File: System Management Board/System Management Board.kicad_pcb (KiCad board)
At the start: 2 copper layers, 116.8 x 142.2 mm, 9 parts, among them J6 Conn_02x20_Odd_Even, K1 J115F11CH5VDCS61.5U, K2 J114FL1CS165VDC.41, K3 J114FL1CS165VDC.41, U1 SC0915, U2 OKI-78SR-5/1.5-W36E-C, U3 OKI-78SR-5/1.5-W36E-C

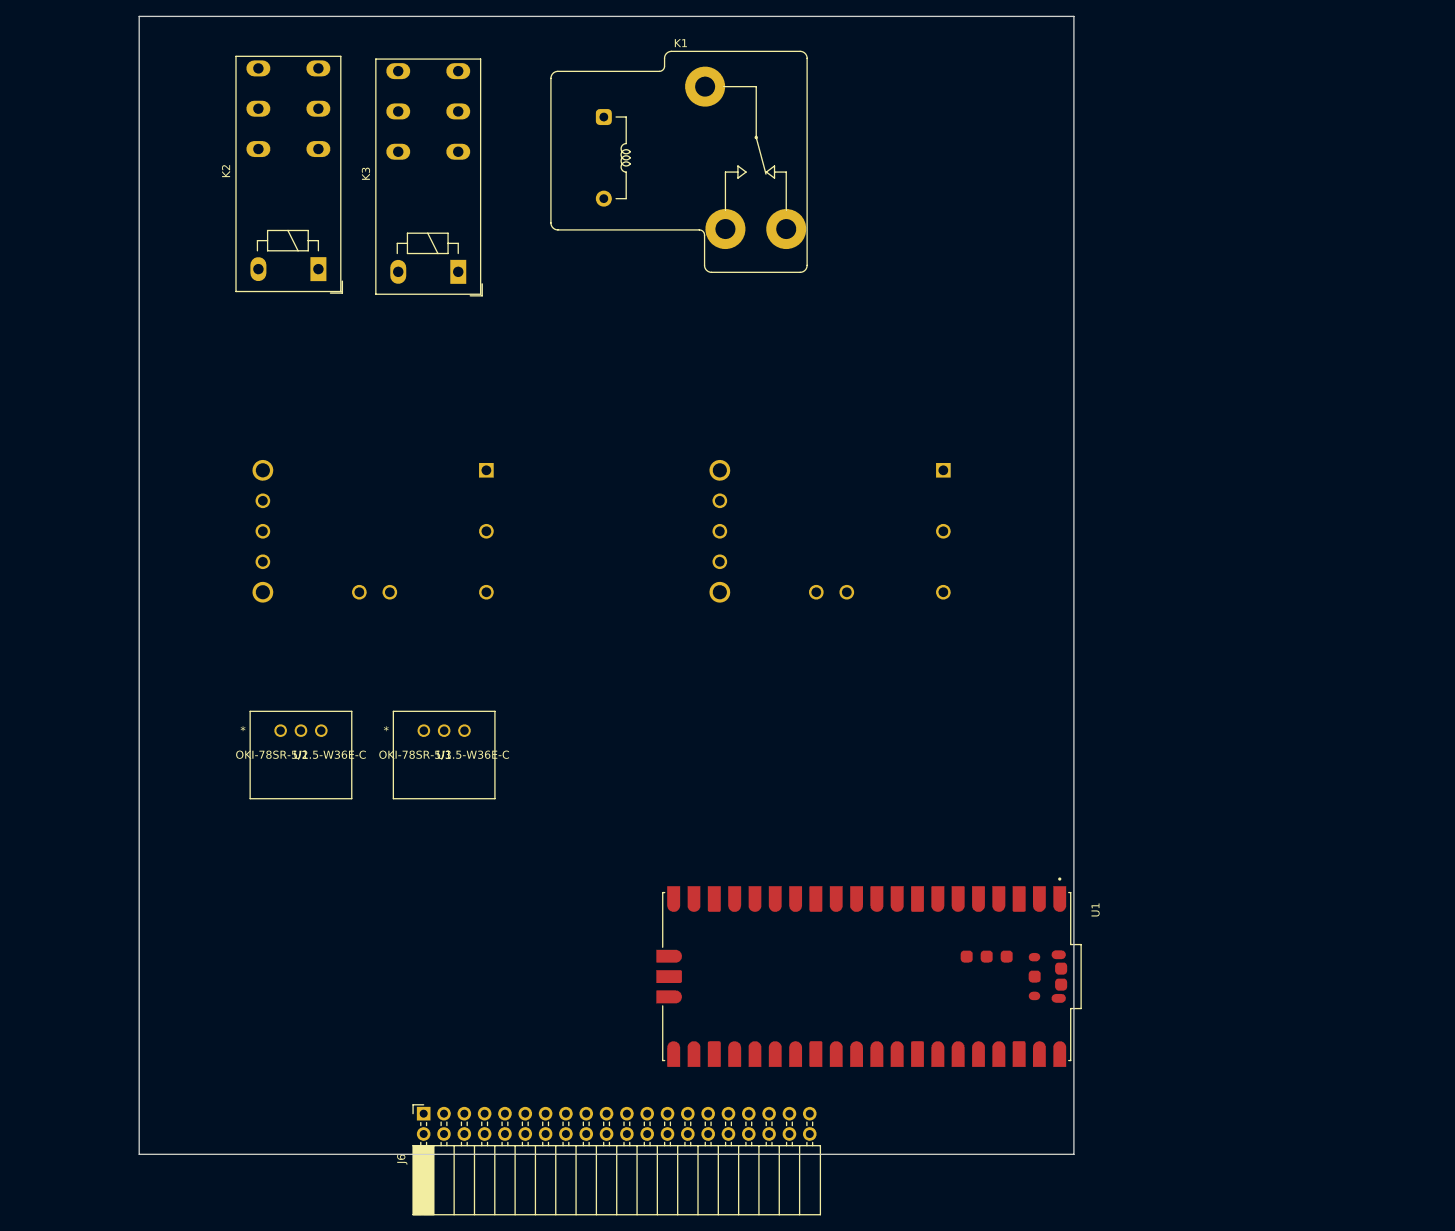
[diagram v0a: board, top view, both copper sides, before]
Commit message: Fixed solidworks brainmelt from last commit and moved PCb template into Kicad
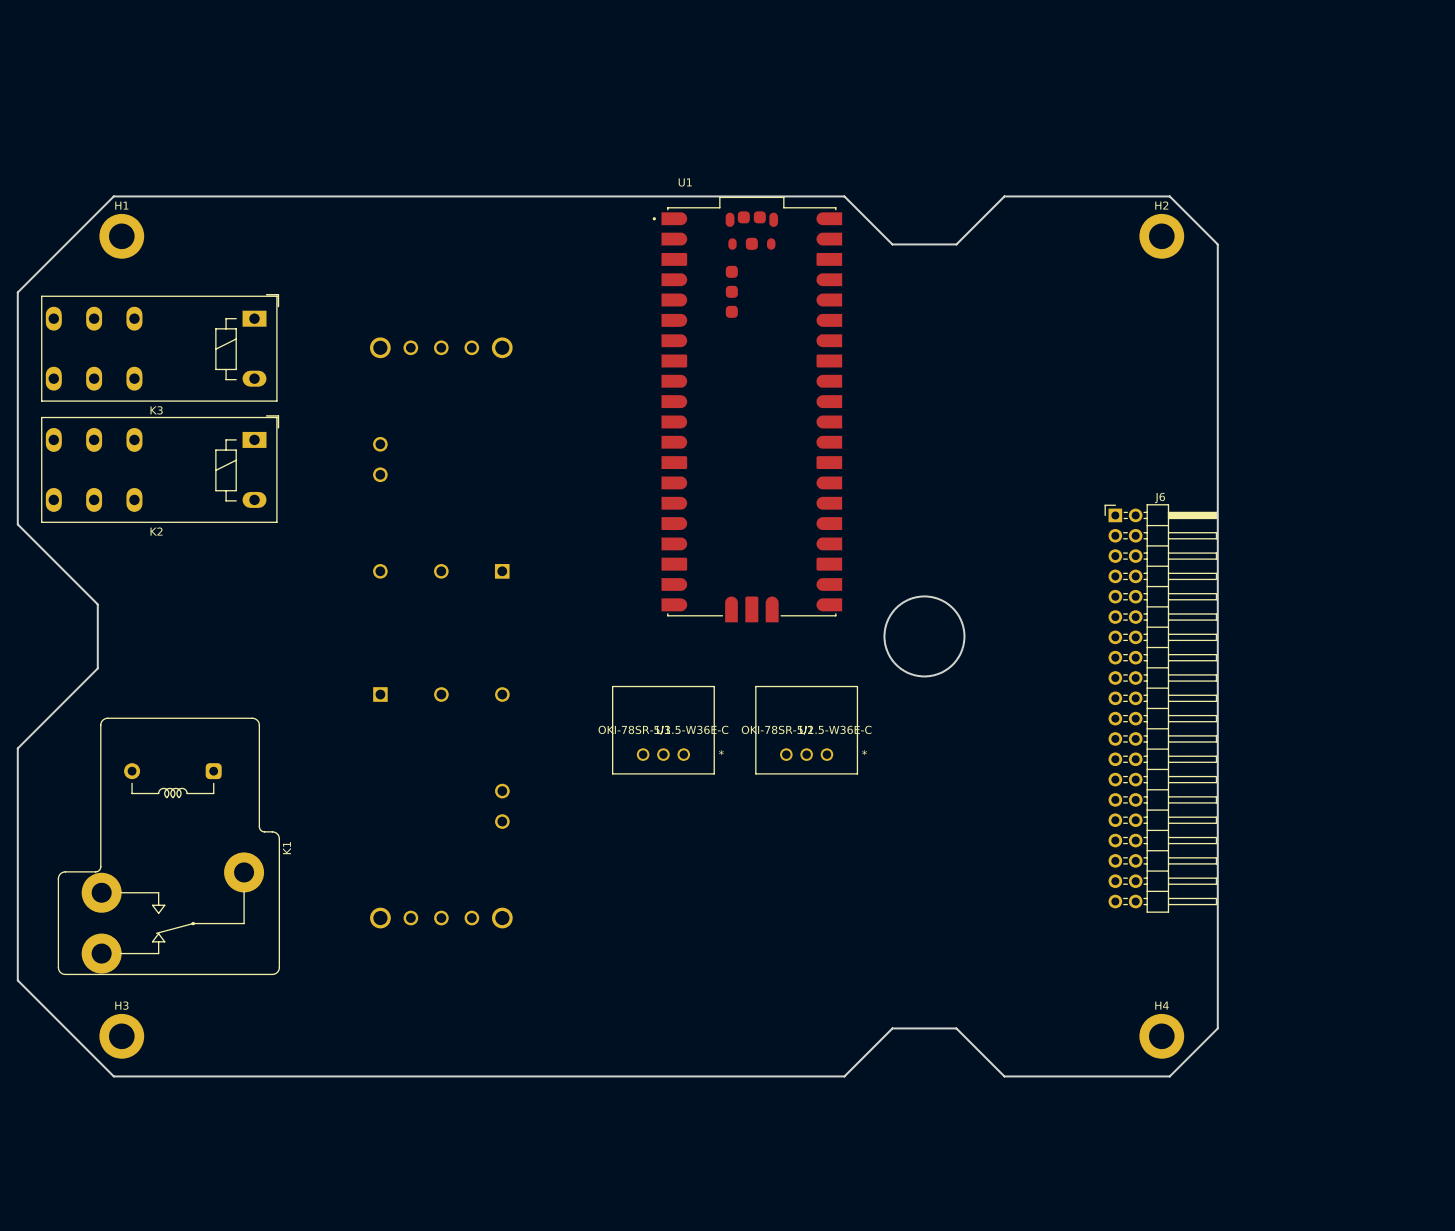
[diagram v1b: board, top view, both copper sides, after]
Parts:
- added H1: MountingHole_Pad, MountingHole:MountingHole_3.2mm_M3_DIN965_Pad, F.Cu at (86.7, 50.4)
- added H2: MountingHole_Pad, MountingHole:MountingHole_3.2mm_M3_DIN965_Pad, F.Cu at (216.7, 50.4)
- added H3: MountingHole_Pad, MountingHole:MountingHole_3.2mm_M3_DIN965_Pad, F.Cu at (86.7, 150.3)
- added H4: MountingHole_Pad, MountingHole:MountingHole_3.2mm_M3_DIN965_Pad, F.Cu at (216.7, 150.3)
- J6: footprint Connector_PinSocket_2.54mm:PinSocket_2x20_P2.54mm_Horizontal -> Connector_PinHeader_2.54mm:PinHeader_2x20_P2.54mm_Horizontal
- moved J6 114.3 mm to (210.9, 85.2), turned to 0 degrees
- moved K1 90.2 mm to (93.1, 114.7), turned to -90 degrees
- moved PS2 75.7 mm to (119.1, 107.6), turned to -90 degrees
- moved U1 72.0 mm to (165.5, 72.3), turned to 0 degrees
- moved U2 68.4 mm to (174.9, 115.1), turned to 180 degrees
- moved U3 32.6 mm to (157.0, 115.1), turned to 180 degrees
- moved K3 25.8 mm to (103.6, 60.6), turned to 180 degrees
- moved K2 22.5 mm to (103.6, 75.8), turned to 180 degrees
- moved PS1 12.8 mm to (134.3, 92.2), turned to 90 degrees
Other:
- board size 116.8 x 142.2 mm -> 150 x 110 mm
- copper layers 2 -> 4

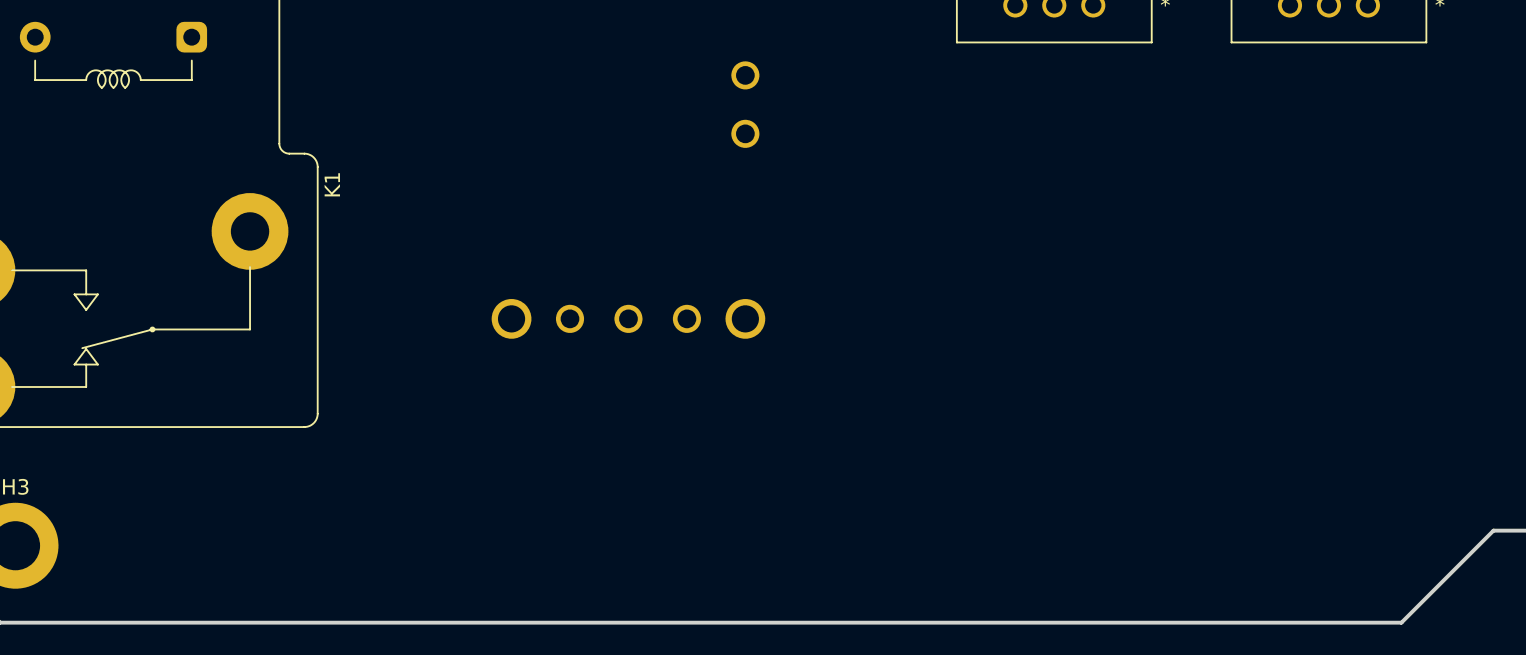
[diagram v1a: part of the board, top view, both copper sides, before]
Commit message: Worked on importing KiCad parts and major componet layout
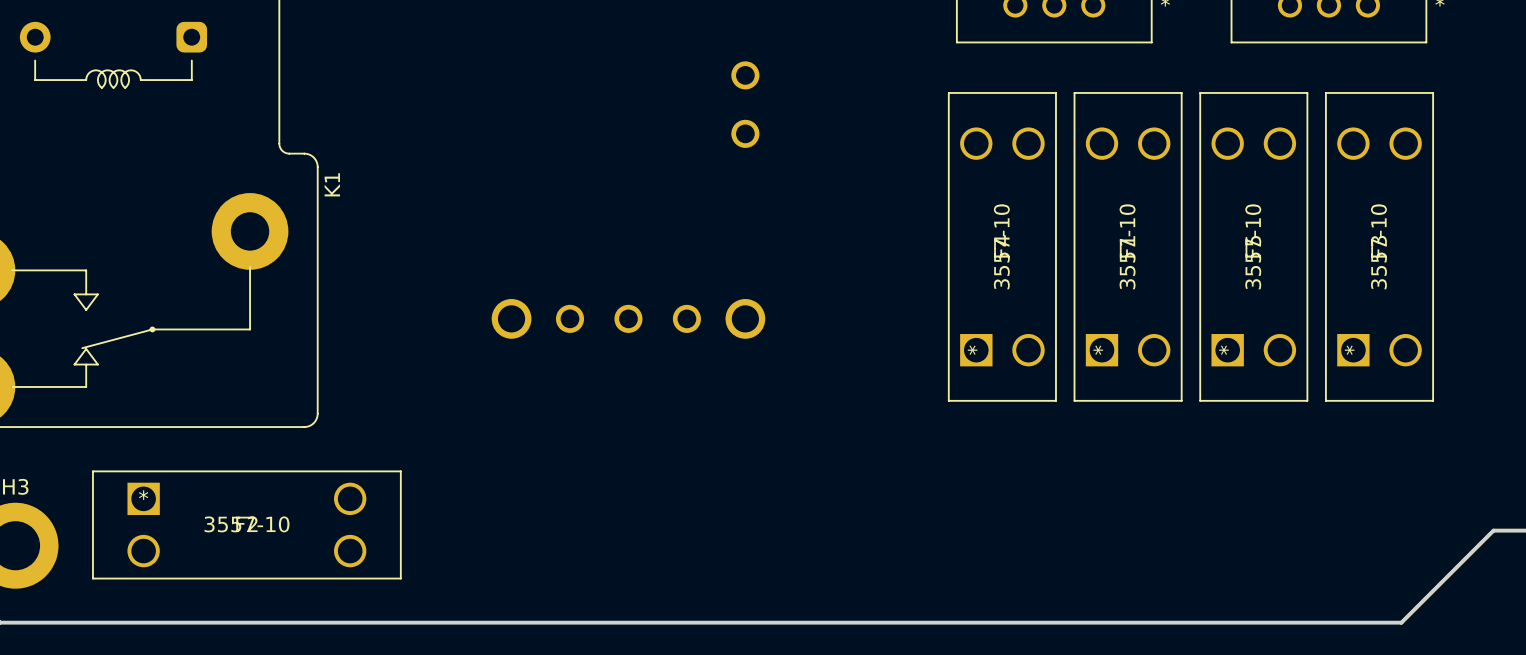
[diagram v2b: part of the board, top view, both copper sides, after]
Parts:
- added F1: 3557-10, SMB:3557-10, F.Cu at (157.5, 137.6)
- added F2: 3557-10, SMB:3557-10, F.Cu at (95.1, 147.3)
- added F3: 3557-10, SMB:3557-10, F.Cu at (173.9, 137.6)
- added F4: 3557-10, SMB:3557-10, F.Cu at (149.3, 137.6)
- added F5: 3557-10, SMB:3557-10, F.Cu at (165.7, 137.6)

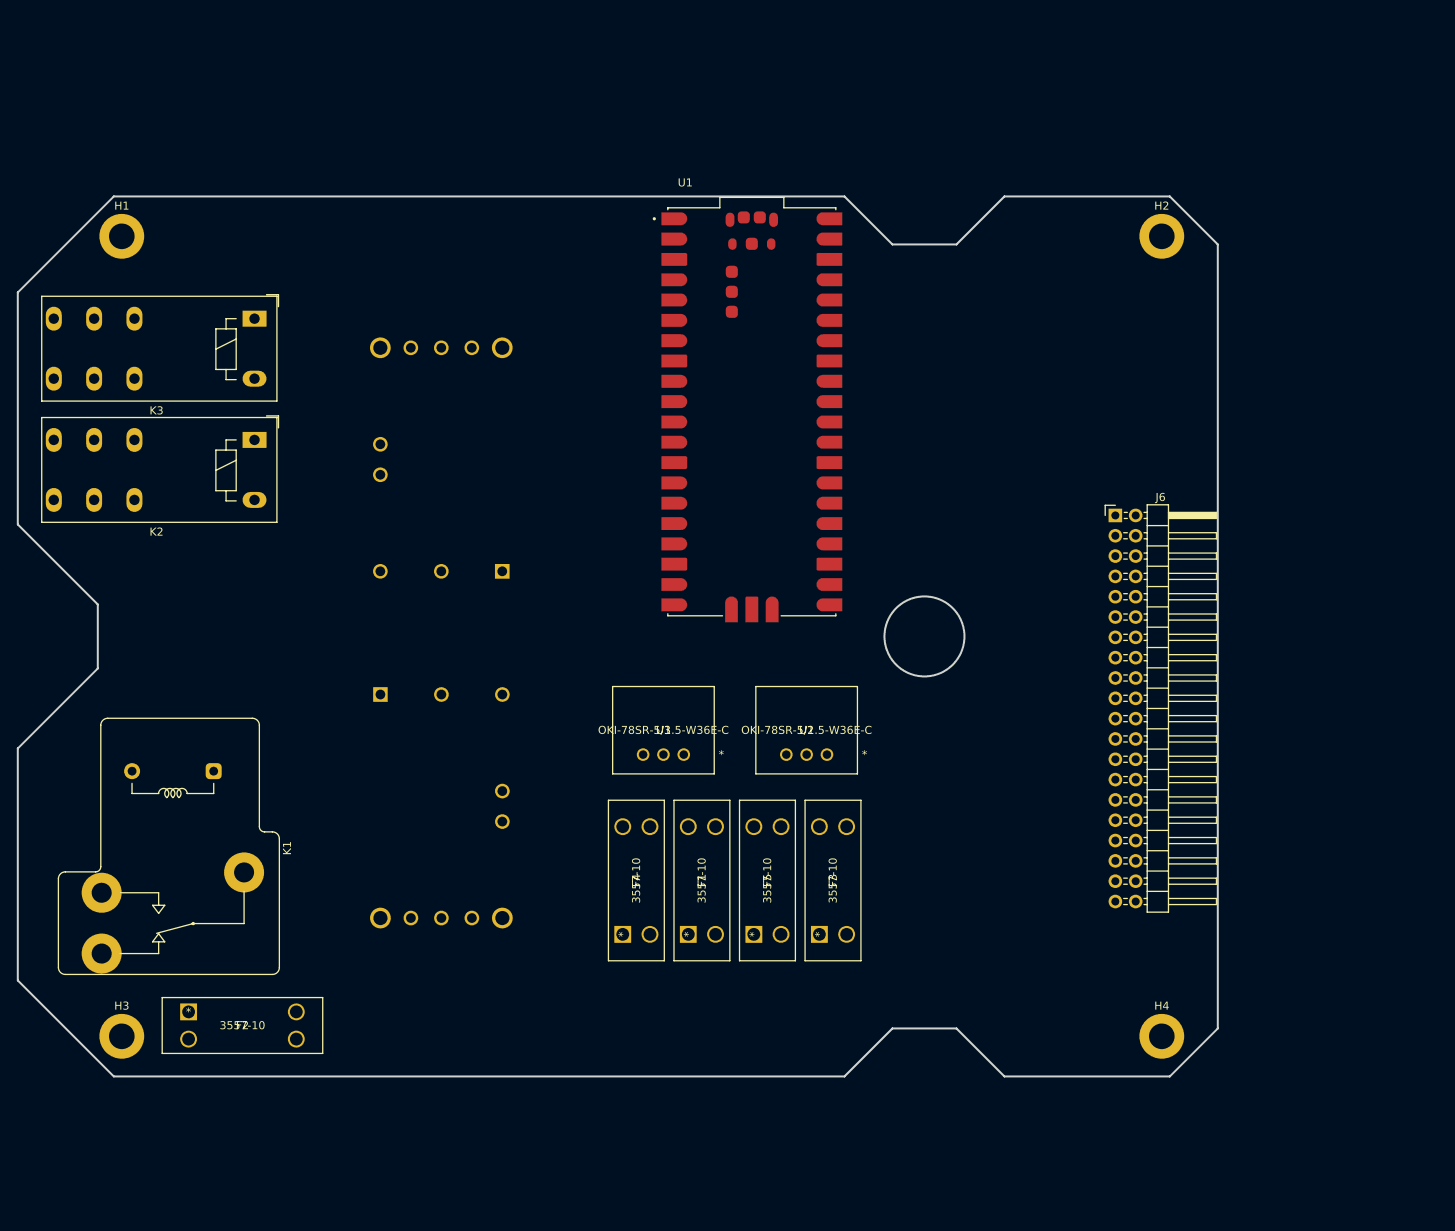
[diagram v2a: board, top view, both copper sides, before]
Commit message: Added more parts to SMB KiCad, worked on schematic and power supplies
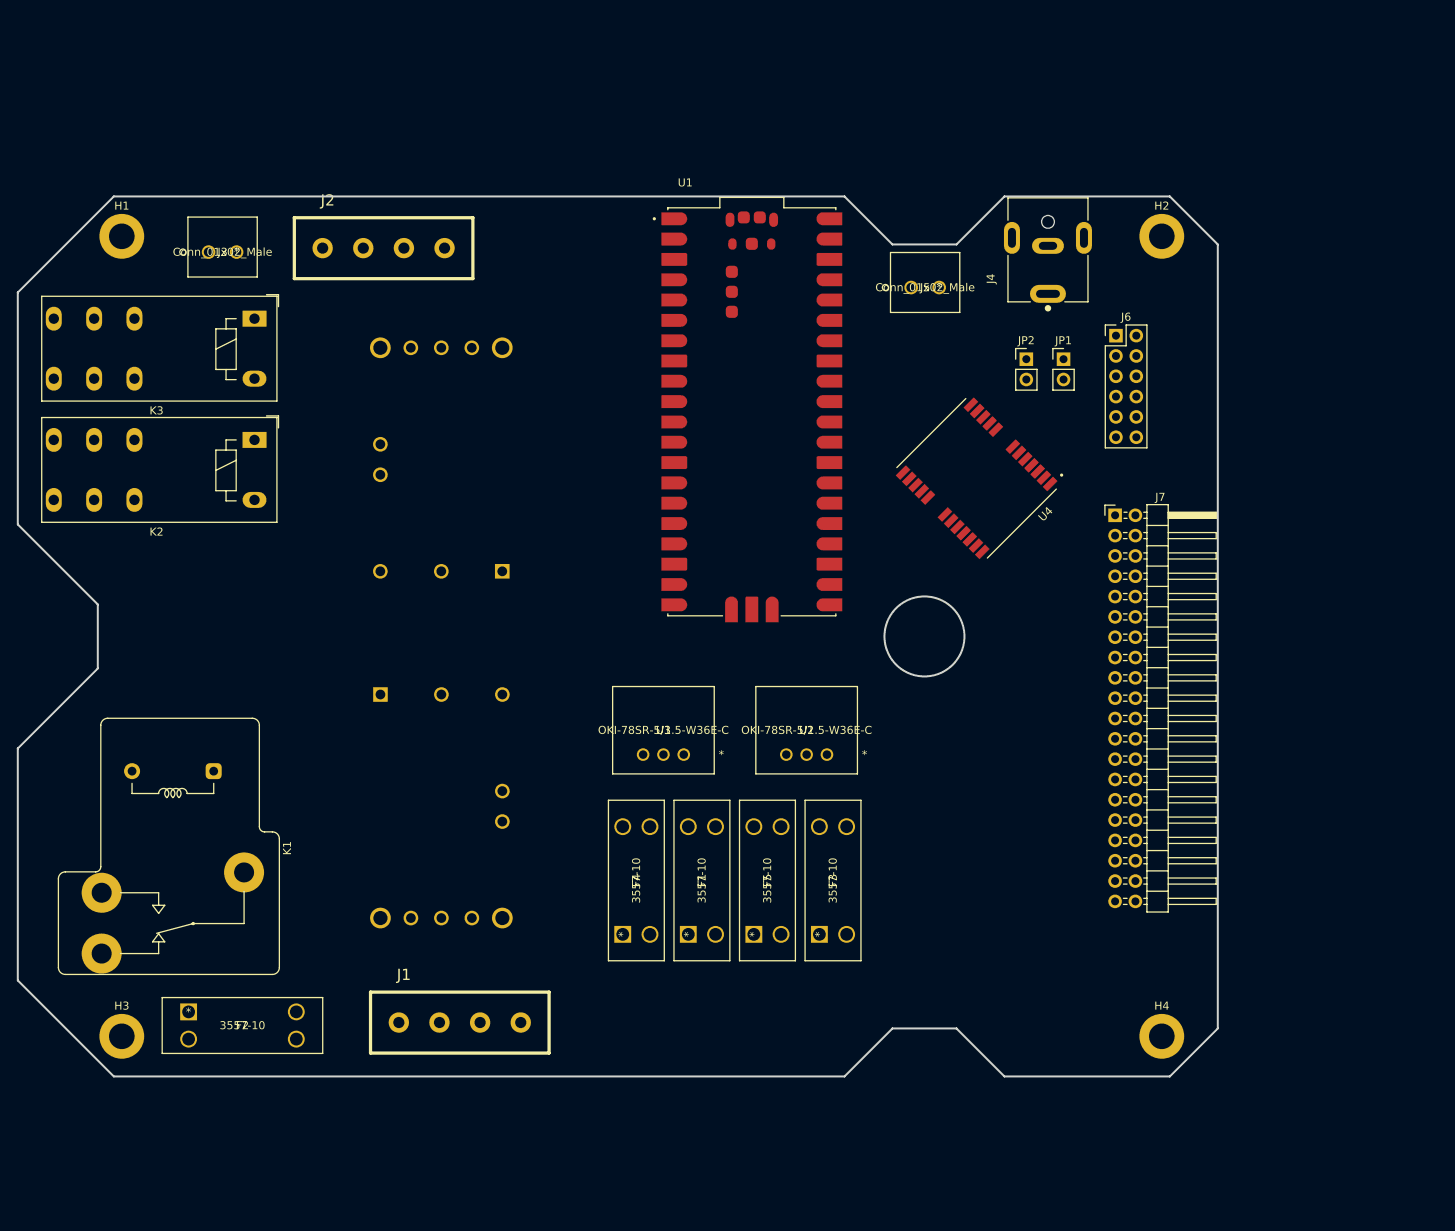
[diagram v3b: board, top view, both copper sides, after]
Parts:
- added J1: Conn_01x04_Male, SMB:1924321, F.Cu at (129.0, 148.6)
- added J2: Conn_01x04_Male, SMB:1924321, F.Cu at (119.5, 51.8)
- added J3: Conn_01x02_Male, SMB:1843606, F.Cu at (101.1, 52.3)
- added J4: PJ-063BH, SMB:CUI_PJ-063BH, F.Cu at (202.5, 57.5)
- added J5: Conn_01x02_Male, SMB:1843606, F.Cu at (188.9, 56.8)
- added J7: Conn_02x20_Odd_Even, Connector_PinHeader_2.54mm:PinHeader_2x20_P2.54mm_Horizontal, F.Cu at (210.9, 85.2)
- added JP1: Jumper_2_Open, Connector_PinHeader_2.54mm:PinHeader_1x02_P2.54mm_Vertical, F.Cu at (204.4, 65.7)
- added JP2: Jumper_2_Open, Connector_PinHeader_2.54mm:PinHeader_1x02_P2.54mm_Vertical, F.Cu at (199.8, 65.7)
- added U4: NEO-M9N-00B, SMB:XCVR_NEO-M9N-00B, F.Cu at (193.6, 80.6)
- J6: value Conn_02x20_Odd_Even -> Conn_02x06_Counter_Clockwise; footprint Connector_PinHeader_2.54mm:PinHeader_2x20_P2.54mm_Horizontal -> Connector_PinHeader_2.54mm:PinHeader_2x06_P2.54mm_Vertical
- moved J6 22.5 mm to (211.0, 62.8)
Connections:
- J6 pad 1: unconnected-(J6-Pad1) -> GND
- J6 pad 10: unconnected-(J6-Pad10) -> Net-(J6-Pad10)
- J6 pad 12: unconnected-(J6-Pad12) -> GND
- J6 pad 2: unconnected-(J6-Pad2) -> JET_RECOV
- J6 pad 3: unconnected-(J6-Pad3) -> JET_RST
- J6 pad 4: unconnected-(J6-Pad4) -> JET_PWR
- J6 pad 5: unconnected-(J6-Pad5) -> Net-(J6-Pad5)
- J6 pad 6: unconnected-(J6-Pad6) -> Net-(J6-Pad6)
- J6 pad 7: unconnected-(J6-Pad7) -> CVB_STBY
- J6 pad 8: unconnected-(J6-Pad8) -> SYSTEM_OC
- J6 pad 9: unconnected-(J6-Pad9) -> Net-(J6-Pad9)
